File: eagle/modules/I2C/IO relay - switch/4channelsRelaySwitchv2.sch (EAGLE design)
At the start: 39 parts, among them IC2 MCP2300X/P, IC3 ULN2803, K1 JS-M1-9V-5, K2 JS-M1-9V-5, K3 JS-M1-9V-5, K4 JS-M1-9V-5, P1 WIREPAD3,81/1,4, P2 WIREPAD3,81/1,4, P3 WIREPAD3,81/1,4, P4 WIREPAD3,81/1,4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

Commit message: Correct bug with pin 6 to 5V
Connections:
- net +5V: now also IC2./RST
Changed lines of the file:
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@@
 <pinref part="P+6" gate="1" pin="+5V"/>
 <wire x1="109.22" y1="129.54" x2="114.3" y2="129.54" width="0.1524" layer="91"/>
+<pinref part="IC2" gate="G$1" pin="/RST"/>
+<wire x1="93.98" y1="119.38" x2="93.98" y2="129.54" width="0.1524" layer="91"/>
+<wire x1="93.98" y1="129.54" x2="109.22" y2="129.54" width="0.1524" layer="91"/>
 </segment>
 </net>

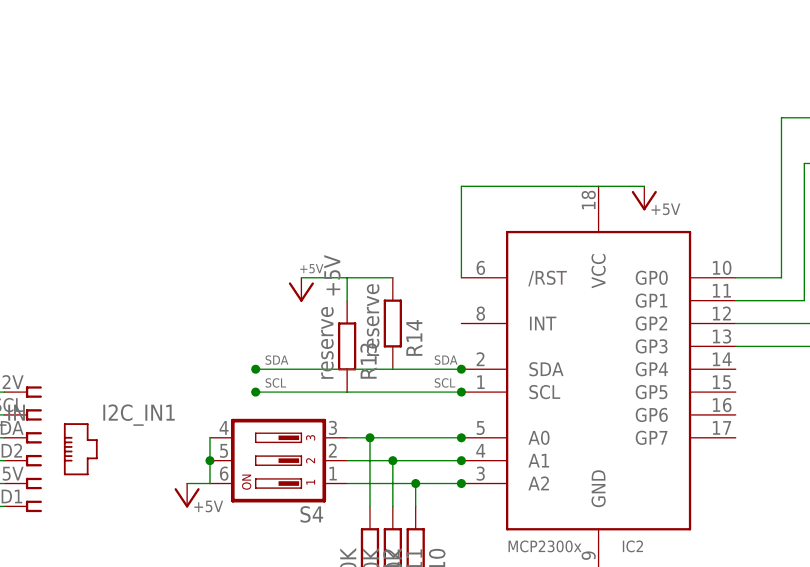
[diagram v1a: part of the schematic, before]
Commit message: update RESET pin to put a resistor of 10k to +5V
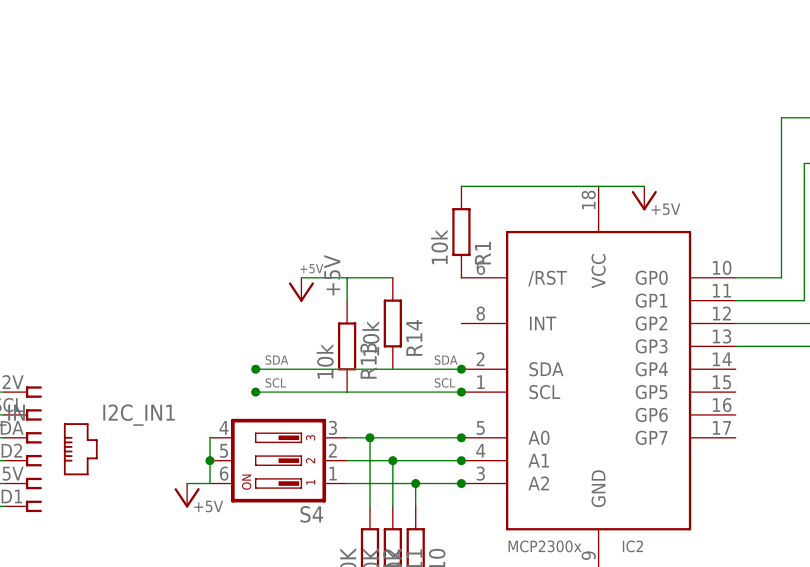
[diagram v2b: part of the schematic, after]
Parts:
- added R1: 10k, resistor:R-EU_M1206
- R13, R14: value reserve -> 10k
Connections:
- new net N$21: IC2./RST, R1.1
- net +5V: now also R1.2; no longer IC2./RST
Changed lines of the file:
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@@
 <part name="C2" library="rcl" deviceset="C-EU" device="C1206" value="100nF"/>
 <part name="C3" library="rcl" deviceset="CPOL-EU" device="E3.5-8" value="5uF 50V"/>
-<part name="R13" library="resistor" deviceset="R-EU_" device="M1206" value="reserve"/>
-<part name="R14" library="resistor" deviceset="R-EU_" device="M1206" value="reserve"/>
+<part name="R13" library="resistor" deviceset="R-EU_" device="M1206" value="10k"/>
+<part name="R14" library="resistor" deviceset="R-EU_" device="M1206" value="10k"/>
 <part name="P+8" library="supply1" deviceset="+5V" device=""/>
 <part name="P+1" library="supply1" deviceset="+5V" device=""/>
@@
 <part name="P7" library="wirepad" deviceset="WIREPAD" device="3,81/1,4"/>
 <part name="P8" library="wirepad" deviceset="WIREPAD" device="3,81/1,4"/>
+<part name="R1" library="resistor" deviceset="R-EU_" device="M1206" value="10k"/>
 </parts>
 <sheets>
@@
 <instance part="P7" gate="G$1" x="261.62" y="160.02" rot="R180"/>
 <instance part="P8" gate="G$1" x="261.62" y="182.88" rot="R180"/>
+<instance part="R1" gate="G$1" x="93.98" y="124.46" rot="MR90"/>
 </instances>
 <busses>
@@
 <pinref part="P+6" gate="1" pin="+5V"/>
 <wire x1="109.22" y1="129.54" x2="114.3" y2="129.54" width="0.1524" layer="91"/>
-<pinref part="IC2" gate="G$1" pin="/RST"/>
-<wire x1="93.98" y1="119.38" x2="93.98" y2="129.54" width="0.1524" layer="91"/>
 <wire x1="93.98" y1="129.54" x2="109.22" y2="129.54" width="0.1524" layer="91"/>
+<pinref part="R1" gate="G$1" pin="2"/>
 </segment>
 </net>
@@
 </segment>
 </net>
+<net name="N$21" class="0">
+<segment>
+<pinref part="IC2" gate="G$1" pin="/RST"/>
+<pinref part="R1" gate="G$1" pin="1"/>
+</segment>
+</net>
